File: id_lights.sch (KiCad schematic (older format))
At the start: 26 parts

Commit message: Continued syncing with original design.
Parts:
- removed C?: C, ~, symbol C
- removed F? (x4): FUSE, ~, symbol FUSE
- removed K?: CONN_3, symbol CONN_3
- removed P?: CONN_4, symbol CONN_4
- removed Q?: FET_N_GDS, symbol FET_N_GDS
- removed R?: R, ~, symbol R
- removed U? (x4): 74LS74, ~, symbol 74LS74
- added C12: C, ~, symbol C
- added F19, F21, F23: 1.6A 24V, ~, symbol FUSE
- added F22: 1.1A 24V, ~, symbol FUSE
- added J18: JST-PA-3, ~, symbol CONN_3
- added J20: JST-PA-4, ~, symbol CONN_4
- added Q2: FET_N_GDS, symbol FET_N_GDS
- added R21: R, ~, symbol R
- added U3, U7: 74LS74, ~, symbol 74LS74
- F18: renamed from F?; value FUSE -> 1.6A 24V; Digikey (none) -> F2870CT-ND
- F20: renamed from F?; value FUSE -> 1.1A 24V; Digikey (none) -> F2868CT-ND
- J17: renamed from K?; value CONN_3 -> JST-PA-3; footprint (none) -> ~; Digikey (none) -> 455-2644-1-ND
- J19: renamed from P?; value CONN_4 -> JST-PA-4; footprint (none) -> ~; Digikey (none) -> 455-2645-1-ND
- gave numbers to parts that had none: 9
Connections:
- wire segments 94 -> 106

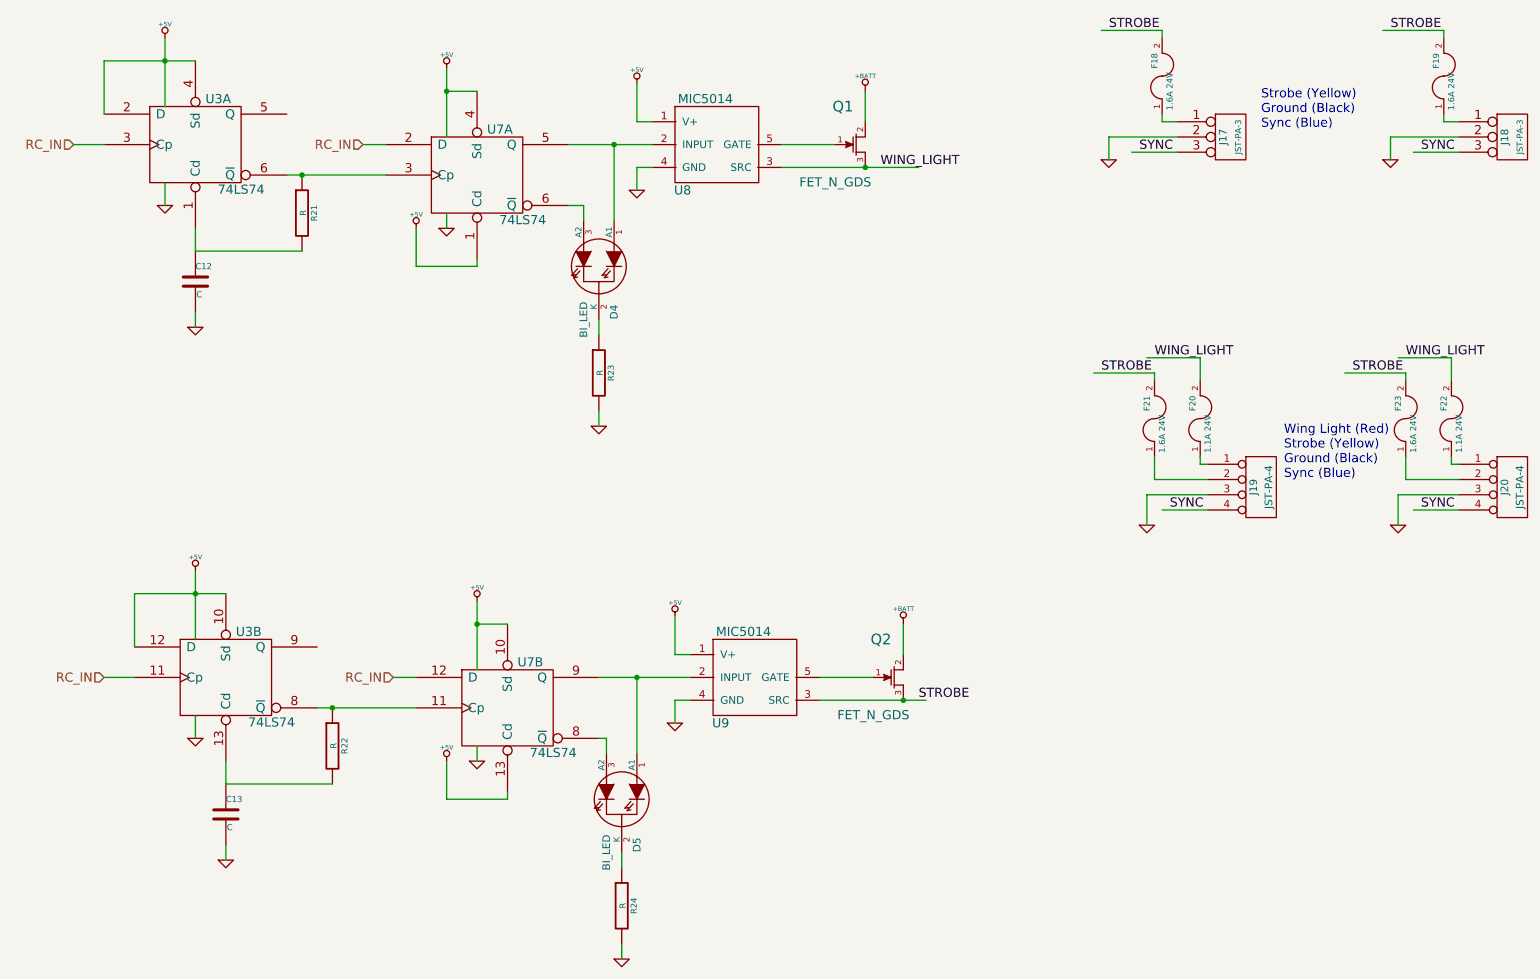
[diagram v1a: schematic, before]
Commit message: Finishing bom integration with schematic.
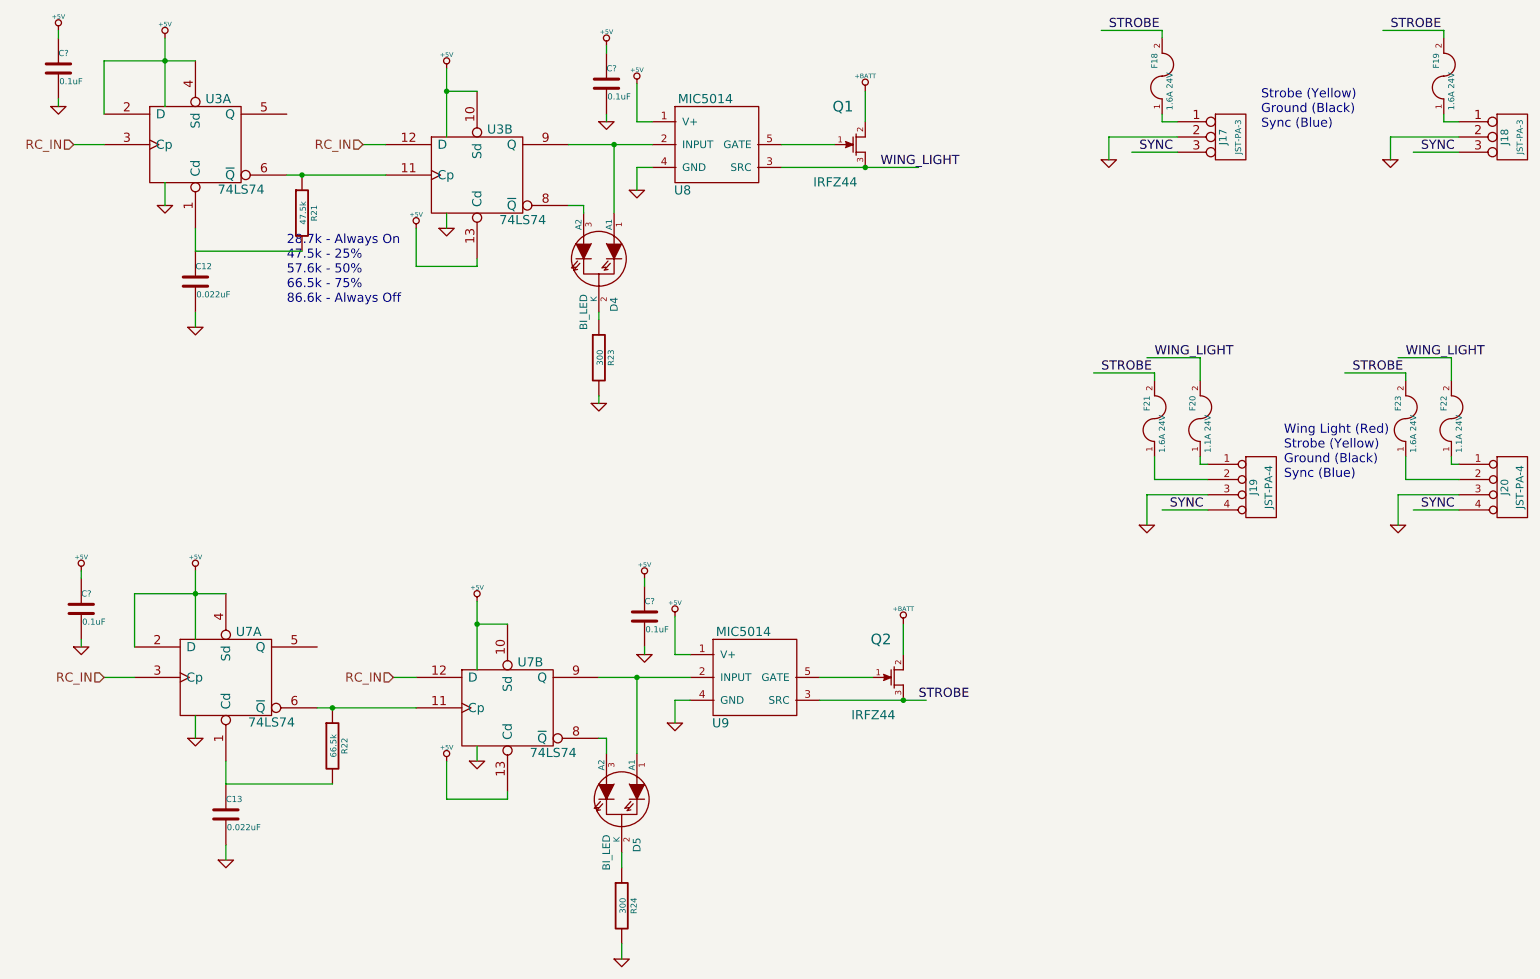
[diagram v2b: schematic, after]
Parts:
- added C? (x4): 0.1uF, SM0805, symbol C
- C12, C13: value C -> 0.022uF; Digikey (none) -> 490-8308-1-ND
- D4, D5: Digikey (none) -> VLMV3100-GS08CT-ND
- Q1, Q2: value FET_N_GDS -> IRFZ44; footprint (none) -> ~; Digikey (none) -> IRFZ44STRRPBFCT-ND
- R21: value R -> 47.5k; Digikey (none) -> P47.5KDACT-ND
- R22: value R -> 66.5k; Digikey (none) -> P66.5KDACT-ND
- R23, R24: value R -> 300; Digikey (none) -> P300CCT-ND
- U3, U7: Digikey (none) -> 296-1079-1-ND
- U3: renamed from U7; Digikey (none) -> 296-1079-1-ND
- U7: renamed from U3; Digikey (none) -> 296-1079-1-ND
- U8, U9: Digikey (none) -> 576-1233-1-ND
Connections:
- wire segments 106 -> 114
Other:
- note added: "28.7k - Always On\n47.5k - 25%\n57.6k - 50%\n66.5k - 75%\n86.6k - Always Off"
- moved on the sheet: D4, R23

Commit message: Adding buffer on voltage reference output.
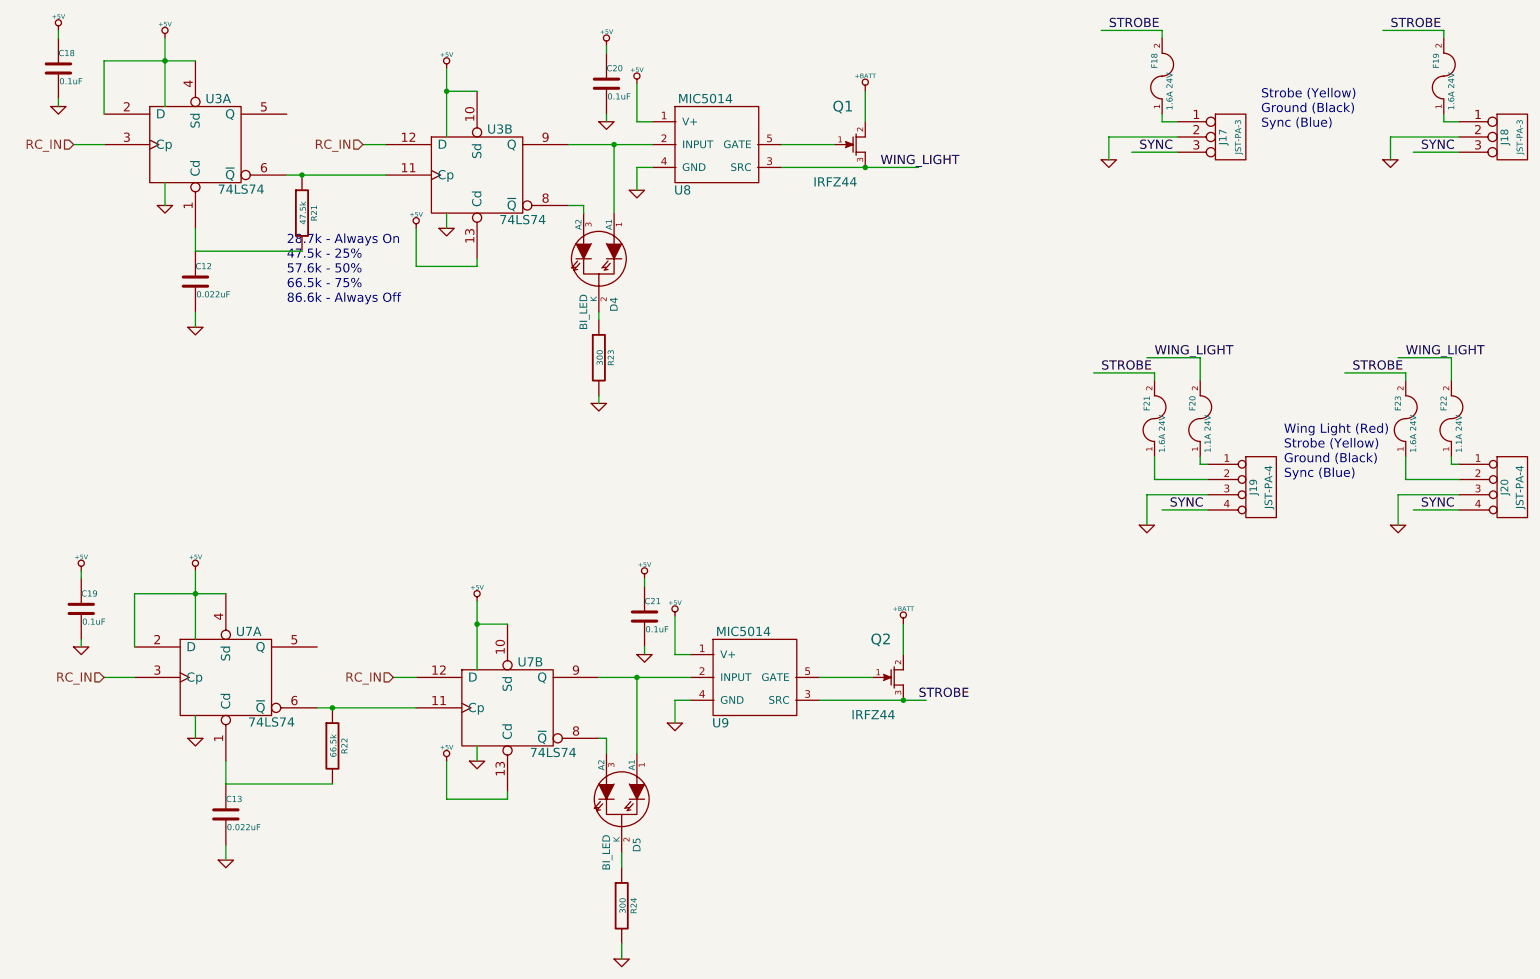
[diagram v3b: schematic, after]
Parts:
- gave numbers to parts that had none: 4
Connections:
- wire segments 114 -> 102
